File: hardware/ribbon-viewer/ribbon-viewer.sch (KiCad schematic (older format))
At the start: 186 parts, among them J1 Conn_01x40, J2 Conn_01x40, J3 Power, U1 74HC541, U2 74HC541, U3 74HC541, U4 74HC541, U5 74HC541, U6 MCP1825S

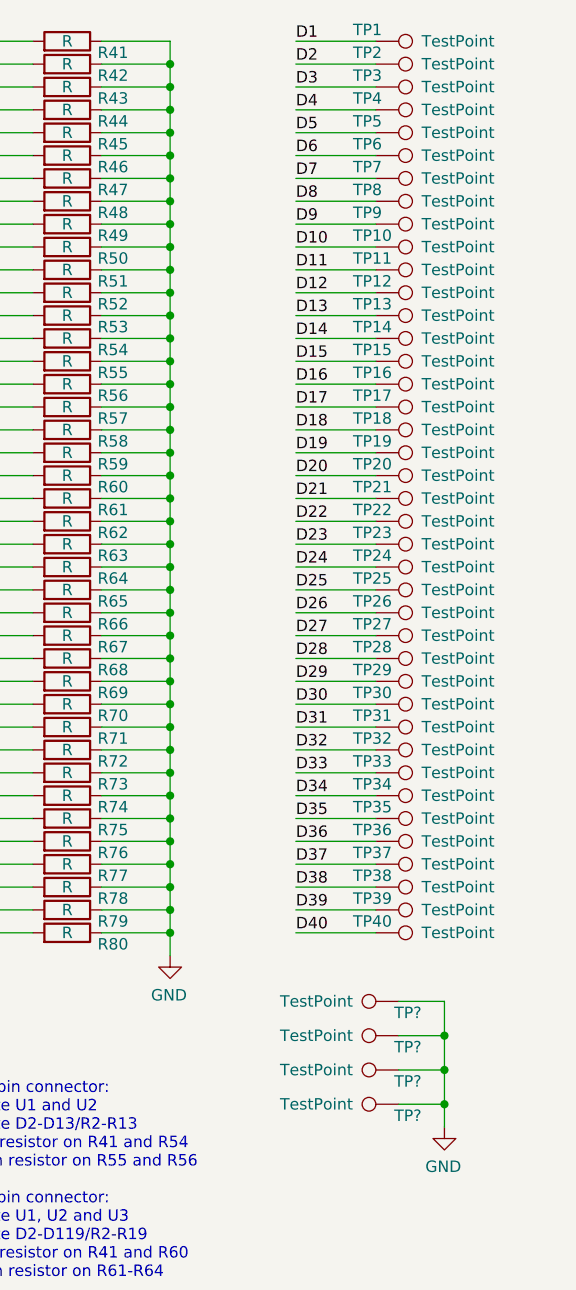
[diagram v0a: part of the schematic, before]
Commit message: Change testpoints to pin header
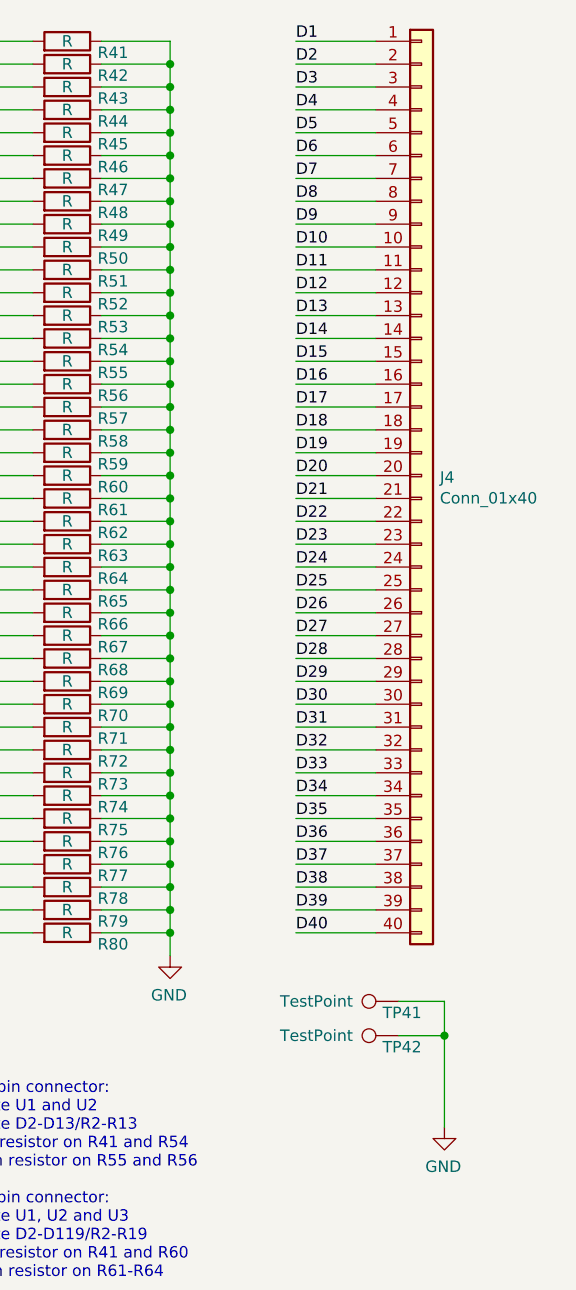
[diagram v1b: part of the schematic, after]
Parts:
- removed TP1, TP10, TP11, TP12, TP13, TP14, TP15, TP16, TP17, TP18, TP19, TP2, TP20, TP21, TP22, TP23, TP24, TP25, TP26, TP27, TP28, TP29, TP3, TP30, TP31, TP32, TP33, TP34, TP35, TP36, TP37, TP38, TP39, TP4, TP40, TP5, TP6, TP7, TP8, TP9: TestPoint, riscv-serial:TestPoint-0805, symbol Connector:TestPoint
- removed TP? (x2): TestPoint, TestPoint:TestPoint_THTPad_2.0x2.0mm_Drill1.0mm, symbol Connector:TestPoint
- added J4: Conn_01x40, Connector_PinHeader_2.54mm:PinHeader_2x20_P2.54mm_Vertical, symbol Connector_Generic:Conn_01x40
- gave numbers to parts that had none: 2
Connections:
- net D1: now also J4.1 (Pin_1)
- net D10: now also J4.10 (Pin_10)
- net D11: now also J4.11 (Pin_11)
- net D12: now also J4.12 (Pin_12)
- net D13: now also J4.13 (Pin_13)
- net D14: now also J4.14 (Pin_14)
- net D15: now also J4.15 (Pin_15)
- net D16: now also J4.16 (Pin_16)
- net D17: now also J4.17 (Pin_17)
- net D18: now also J4.18 (Pin_18)
- net D19: now also J4.19 (Pin_19)
- net D2: now also J4.2 (Pin_2)
- net D20: now also J4.20 (Pin_20)
- net D21: now also J4.21 (Pin_21)
- net D22: now also J4.22 (Pin_22)
- net D23: now also J4.23 (Pin_23)
- net D24: now also J4.24 (Pin_24)
- net D25: now also J4.25 (Pin_25)
- net D26: now also J4.26 (Pin_26)
- net D27: now also J4.27 (Pin_27)
- net D28: now also J4.28 (Pin_28)
- net D29: now also J4.29 (Pin_29)
- net D3: now also J4.3 (Pin_3)
- net D30: now also J4.30 (Pin_30)
- net D31: now also J4.31 (Pin_31)
- net D32: now also J4.32 (Pin_32)
- net D33: now also J4.33 (Pin_33)
- net D34: now also J4.34 (Pin_34)
- net D35: now also J4.35 (Pin_35)
- net D36: now also J4.36 (Pin_36)
- net D37: now also J4.37 (Pin_37)
- net D38: now also J4.38 (Pin_38)
- net D39: now also J4.39 (Pin_39)
- net D4: now also J4.4 (Pin_4)
- net D40: now also J4.40 (Pin_40)
- net D5: now also J4.5 (Pin_5)
- net D6: now also J4.6 (Pin_6)
- net D7: now also J4.7 (Pin_7)
- net D8: now also J4.8 (Pin_8)
- net D9: now also J4.9 (Pin_9)
